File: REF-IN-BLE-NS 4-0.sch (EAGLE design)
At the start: 44 parts, among them U1 NRF52832_10QFN48, U2 AEM10941, X1 FA-128-32MHZMF10Z-AJ5

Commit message: Added caps and prettied up
Documentation is still needed, will add that as an issue
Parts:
- added C17, C18: 12pF, resistor:C-USC0603
- added C19, C20: 220uF, resistor:C-USC1206
- added C21, C22, C23, C24, C25: (no value), resistor:C-USC1206
- added C26, C27, C28, C29, C30: (no value), resistor:C-USC1210
- added U$11: SOLDER_BRIGDECLOSED, 00_PF_Nordic:SOLDER_BRIGDECLOSED
- added U$12, U$13, U$14, U$15, U$16, U$17, U$18, U$19, U$20, U$21, U$22: 1MM_PAD, 00_PF_Nordic:1MM_PAD
- added U$23: CAP-XX_A-TYPE, 00_PF_Nordic:CAP-XX_A-TYPE
- added U$24: CAP-XX_S-TYPE, 00_PF_Nordic:CAP-XX_S-TYPE
- added U$25: CAP-XX_W-TYPE, 00_PF_Nordic:CAP-XX_W-TYPE
- added U$26: BZ01_L-TYPE, 00_PF_Nordic:BZ01_L-TYPE
- added U$27: BZ059_N-TYPE, 00_PF_Nordic:BZ059_N-TYPE
- added U$28: BZ01_S-TYPE, 00_PF_Nordic:BZ01_S-TYPE
- added U$29: BZ05_S-TYPE, 00_PF_Nordic:BZ05_S-TYPE
- added U$30: BZ09_S-TYPE, 00_PF_Nordic:BZ09_S-TYPE
- added X2: 32.768k, 00_PF_Nordic:FC-135_32.7680KA-AC
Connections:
- removed net N$34: U2.BAL
- new net BAL: U$11.P1, U$19.P$1, U$23.BAL, U$24.BAL, U$25.BAL, U$26.2, U$28.2, U$29.2, U$30.2, U2.BAL
- new net BATT: C19.1, C20.1, C21.1, C22.1, C23.1, C24.1, C25.1, C26.1, C27.1, C28.1, C29.1, C30.1, U$18.P$1, U$23.+, U$24.+, U$25.+, U$26.1, U$27.1, U$28.1, U$29.1, U$30.1, U2.BATT
- new net N$36: C17.1, U1.P0_XL1, X2.P$1
- new net N$37: C18.1, U1.P1_XL2, X2.P$2
- new net N$38: U$20.P$1, U1.P2_AIN0
- new net N$39: U$13.P$1, U2.STATUS2
- new net N$40: U$14.P$1, U2.STATUS1
- new net N$41: U$15.P$1, U2.STATUS0
- new net N$42: U$21.P$1, U1.P3_AIN1
- new net N$43: U$22.P$1, U1.P4_AIN2
- net GND: now also C17.2, C18.2, C19.2, C20.2, C21.2, C22.2, C23.2, C24.2, C25.2, C26.2, C27.2, C28.2, C29.2, C30.2, U$11.P2, U$17.P$1, U$23.-, U$24.-, U$25.-, U$27.2
- net LVOUT: now also U$16.P$1
- net N$33: now also U$12.P$1, U2.PRIM; no longer U2.BATT
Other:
- note added: "1206 Footprints"
- note added: "1210 Footprints"
- note added: "AVX Super-capacitors"
- note added: "CAP-XX Super-capacitors"
- moved on the sheet: L4, R1, R10, R2, R3, R4, R5, R6, R9, U$1, U2

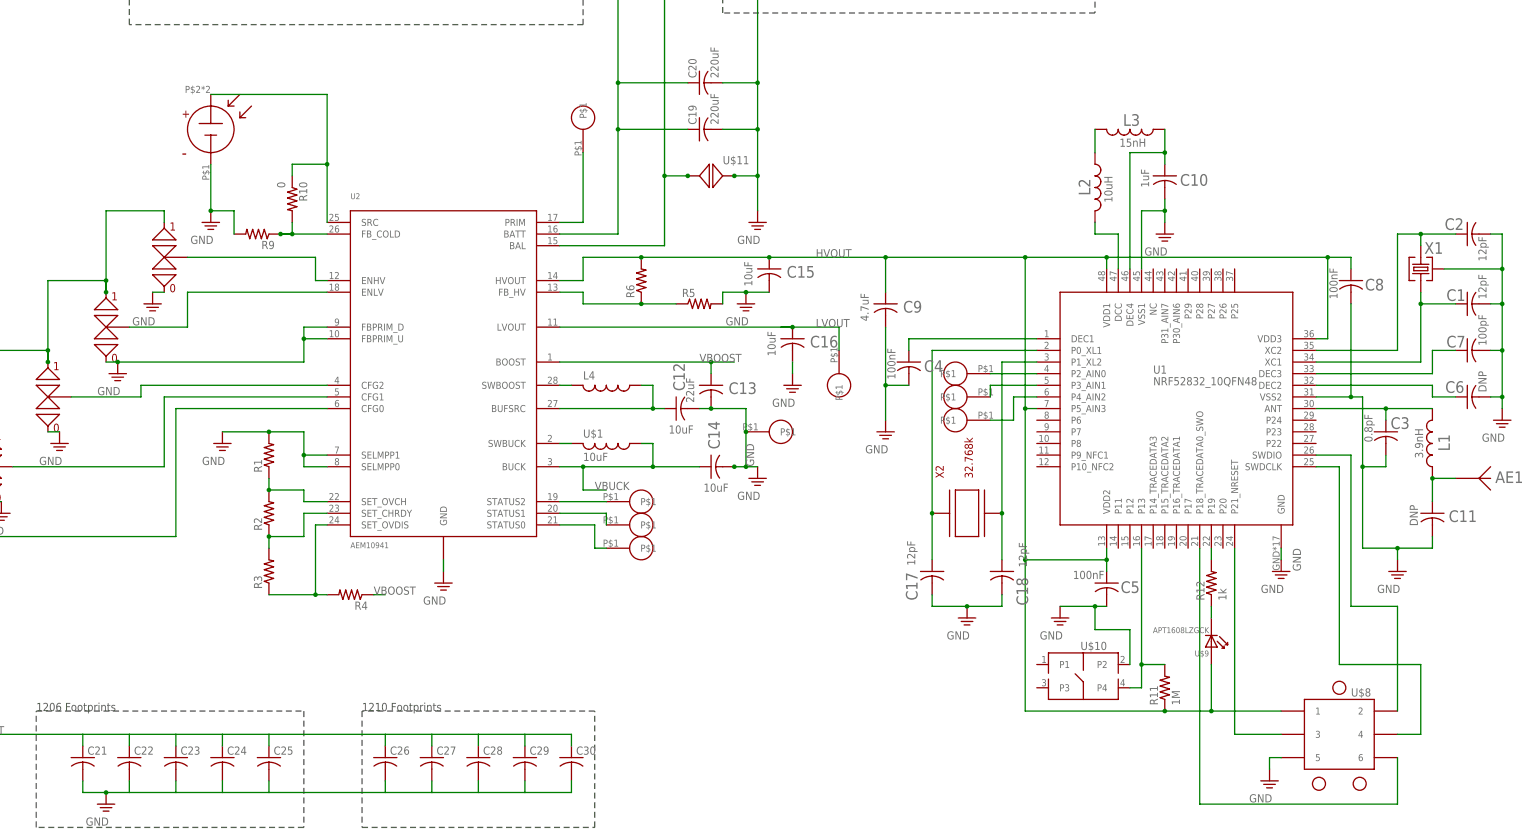
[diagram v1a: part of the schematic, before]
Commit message: Fixed grounding and added labels
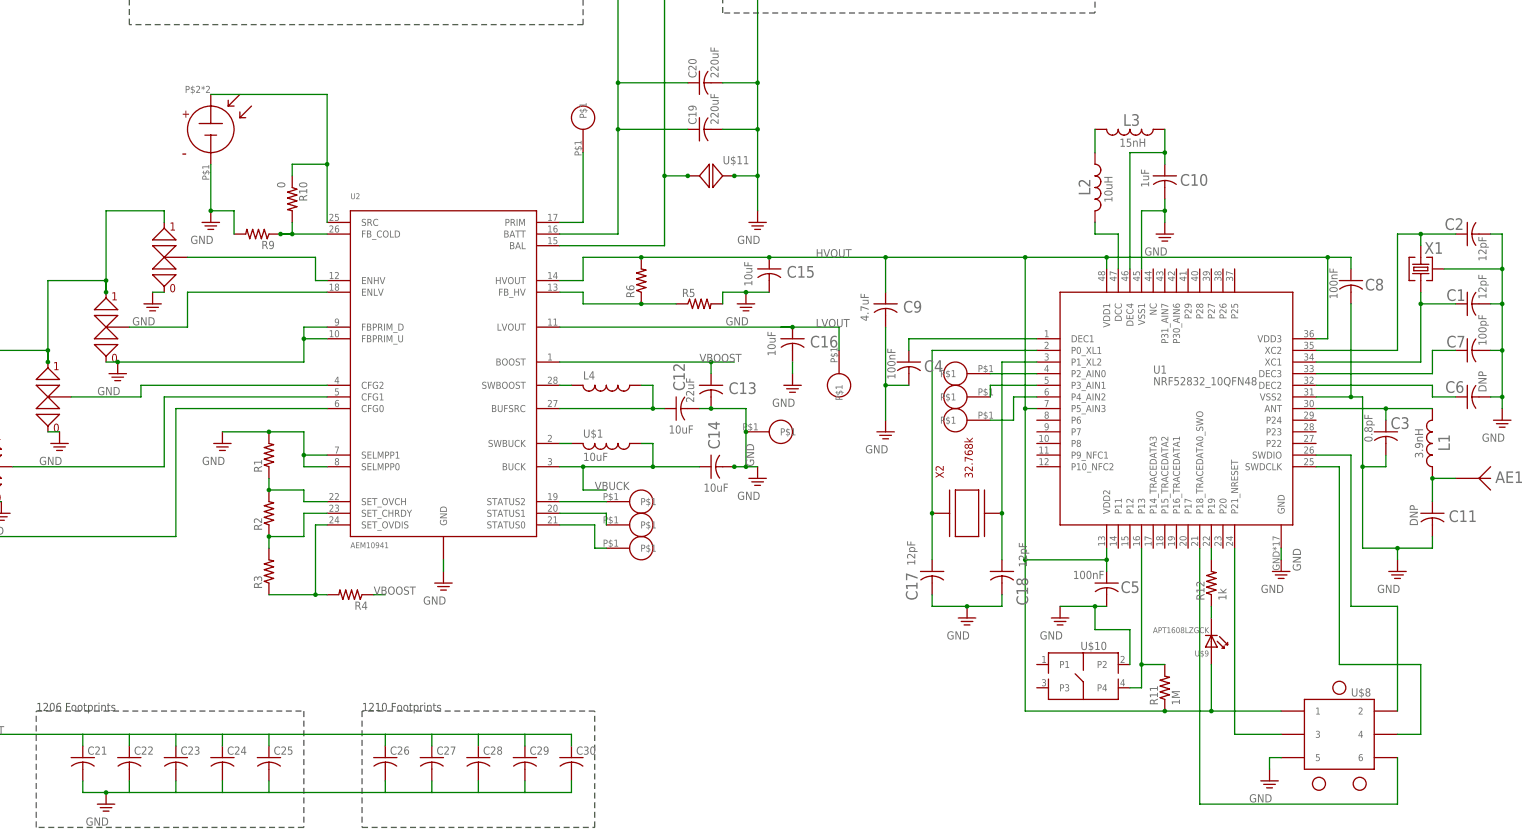
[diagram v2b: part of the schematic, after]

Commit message: Modified top cream
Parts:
- L4: value (none) -> 22uH
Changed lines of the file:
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@@
 <part name="G16" library="supply2" deviceset="PE" device="" value="GND"/>
 <part name="U$7" library="00_PF_Nordic" deviceset="SOLAR_CELL" device=""/>
-<part name="L4" library="00_PF_Nordic" deviceset="744031220" device=""/>
+<part name="L4" library="00_PF_Nordic" deviceset="744031220" device="" value="22uH"/>
 <part name="U$8" library="00_PF_Nordic" deviceset="TC2030-IDC" device=""/>
 <part name="G17" library="supply2" deviceset="PE" device="" value="GND"/>

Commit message: Added MPNs to Device Technologies
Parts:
- C1, C17, C18, C2: device resistor:C-USC0603 -> resistor:C-UST-12PFC0603
- C10: device resistor:C-USC0603 -> resistor:C-UST-1UFC0603; PERCENTAGE (none) -> 10%
- C12, C14, C15, C16: device resistor:C-USC0603 -> resistor:C-UST-10UFC0603
- C13: device resistor:C-USC0603 -> resistor:C-UST-22UFC0603
- C19, C20: device resistor:C-USC1206 -> resistor:C-UST-220UFC1206
- C3: device resistor:C-USC0603 -> resistor:C-UST-0.8PFC0603
- C4, C5, C8: device resistor:C-USC0603 -> resistor:C-UST-100NFC0603
- C7: device resistor:C-USC0603 -> resistor:C-UST-100PFC0603
- C9: device resistor:C-USC0603 -> resistor:C-UST-4.7UFC0603
- L1: device 00_PF_Nordic:L0603 -> 00_PF_Nordic:L0603V-3.9NH
- L2: device 00_PF_Nordic:L0603 -> 00_PF_Nordic:L0603V-10UH
- L3: device 00_PF_Nordic:L0603 -> 00_PF_Nordic:L0603V-15NH
- R10: device resistor:R-US_M0805 -> resistor:R-US_T-0OHMR0805
- R11: device resistor:R-US_M0805 -> resistor:R-US_T-1MOHMR0805
- R12: device resistor:R-US_M0805 -> resistor:R-US_T-1KOHMR0805
- U$1: value 10uF -> 10uH; device 00_PF_Nordic:L1007 -> 00_PF_Nordic:L0603V-10UH; MFG_PART# (none) -> L1007C101KPWST
- U$9: value APT1608LZGCK -> N/A
- X1: value FA-128-32MHZMF10Z-AJ5 -> 32 MHz
- X2: value 32.768k -> 32.768 kHz
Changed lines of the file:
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@@
 <parts>
 <part name="U1" library="00_PF_Nordic" deviceset="NRF52832_10QFN48" device=""/>
-<part name="C1" library="resistor" deviceset="C-US" device="C0603" value="12pF"/>
-<part name="L3" library="00_PF_Nordic" deviceset="L0603" device="" value="15nH"/>
-<part name="L2" library="00_PF_Nordic" deviceset="L0603" device="" value="10uH"/>
-<part name="L1" library="00_PF_Nordic" deviceset="L0603" device="" value="3.9nH"/>
-<part name="C2" library="resistor" deviceset="C-US" device="C0603" value="12pF"/>
-<part name="C3" library="resistor" deviceset="C-US" device="C0603" value="0.8pF"/>
-<part name="C4" library="resistor" deviceset="C-US" device="C0603" value="100nF"/>
-<part name="C5" library="resistor" deviceset="C-US" device="C0603" value="100nF"/>
+<part name="C1" library="resistor" deviceset="C-US" device="C0603" technology="T-12PF" value="12pF"/>
+<part name="L3" library="00_PF_Nordic" deviceset="L0603" device="" technology="V-15NH" value="15nH"/>
+<part name="L2" library="00_PF_Nordic" deviceset="L0603" device="" technology="V-10UH" value="10uH"/>
+<part name="L1" library="00_PF_Nordic" deviceset="L0603" device="" technology="V-3.9NH" value="3.9nH"/>
+<part name="C2" library="resistor" deviceset="C-US" device="C0603" technology="T-12PF" value="12pF"/>
+<part name="C3" library="resistor" deviceset="C-US" device="C0603" technology="T-0.8PF" value="0.8pF"/>
+<part name="C4" library="resistor" deviceset="C-US" device="C0603" technology="T-100NF" value="100nF"/>
+<part name="C5" library="resistor" deviceset="C-US" device="C0603" technology="T-100NF" value="100nF"/>
 <part name="C6" library="resistor" deviceset="C-US" device="C0603" value="DNP"/>
-<part name="C7" library="resistor" deviceset="C-US" device="C0603" value="100pF"/>
-<part name="C8" library="resistor" deviceset="C-US" device="C0603" value="100nF"/>
-<part name="C9" library="resistor" deviceset="C-US" device="C0603" value="4.7uF"/>
-<part name="C10" library="resistor" deviceset="C-US" device="C0603" value="1uF"/>
+<part name="C7" library="resistor" deviceset="C-US" device="C0603" technology="T-100PF" value="100pF"/>
+<part name="C8" library="resistor" deviceset="C-US" device="C0603" technology="T-100NF" value="100nF"/>
+<part name="C9" library="resistor" deviceset="C-US" device="C0603" technology="T-4.7UF" value="4.7uF"/>
+<part name="C10" library="resistor" deviceset="C-US" device="C0603" technology="T-1UF" value="1uF">
+<attribute name="PERCENTAGE" value="10%"/>
+</part>
 <part name="G1" library="supply2" deviceset="PE" device="" value="GND"/>
 <part name="G2" library="supply2" deviceset="PE" device="" value="GND"/>
 <part name="G3" library="supply2" deviceset="PE" device="" value="GND"/>
-<part name="X1" library="00_PF_Nordic" deviceset="FA-128-32MHZMF10Z-AJ5" device=""/>
+<part name="X1" library="00_PF_Nordic" deviceset="FA-128-32MHZMF10Z-AJ5" device="" value="32 MHz"/>
 <part name="G5" library="supply2" deviceset="PE" device="" value="GND"/>
 <part name="G6" library="supply2" deviceset="PE" device="" value="GND"/>
@@
 <part name="C11" library="resistor" deviceset="C-US" device="C0603" value="DNP"/>
 <part name="U2" library="00_PF_Nordic" deviceset="AEM10941" device=""/>
-<part name="C12" library="resistor" deviceset="C-US" device="C0603" value="10uF"/>
+<part name="C12" library="resistor" deviceset="C-US" device="C0603" technology="T-10UF" value="10uF"/>
 <part name="G4" library="supply2" deviceset="PE" device="" value="GND"/>
-<part name="C13" library="resistor" deviceset="C-US" device="C0603" value="22uF"/>
-<part name="C14" library="resistor" deviceset="C-US" device="C0603" value="10uF"/>
-<part name="C15" library="resistor" deviceset="C-US" device="C0603" value="10uF"/>
-<part name="C16" library="resistor" deviceset="C-US" device="C0603" value="10uF"/>
+<part name="C13" library="resistor" deviceset="C-US" device="C0603" technology="T-22UF" value="22uF"/>
+<part name="C14" library="resistor" deviceset="C-US" device="C0603" technology="T-10UF" value="10uF"/>
+<part name="C15" library="resistor" deviceset="C-US" device="C0603" technology="T-10UF" value="10uF"/>
+<part name="C16" library="resistor" deviceset="C-US" device="C0603" technology="T-10UF" value="10uF"/>
 <part name="G7" library="supply2" deviceset="PE" device="" value="GND"/>
 <part name="G8" library="supply2" deviceset="PE" device="" value="GND"/>
 <part name="G9" library="supply2" deviceset="PE" device="" value="GND"/>
-<part name="U$1" library="00_PF_Nordic" deviceset="L1007" device="" value="10uF"/>
+<part name="U$1" library="00_PF_Nordic" deviceset="L0603" device="" technology="V-10UH" value="10uH">
+<attribute name="MFG_PART#" value="L1007C101KPWST"/>
+</part>
 <part name="R1" library="resistor" deviceset="R-US_" device="M0805"/>
 <part name="R2" library="resistor" deviceset="R-US_" device="M0805"/>
@@
 <part name="R6" library="resistor" deviceset="R-US_" device="M0805"/>
 <part name="R9" library="resistor" deviceset="R-US_" device="M0805"/>
-<part name="R10" library="resistor" deviceset="R-US_" device="M0805" value="0"/>
+<part name="R10" library="resistor" deviceset="R-US_" device="R0805" technology="T-0OHM" value="0"/>
 <part name="G16" library="supply2" deviceset="PE" device="" value="GND"/>
 <part name="U$7" library="00_PF_Nordic" deviceset="SOLAR_CELL" device=""/>
@@
 <part name="G17" library="supply2" deviceset="PE" device="" value="GND"/>
 <part name="G18" library="supply2" deviceset="PE" device="" value="GND"/>
-<part name="U$9" library="00_PF_Nordic" deviceset="APT1608LZGCK" device=""/>
-<part name="U$10" library="00_PF_Nordic" deviceset="MJTP1140" device=""/>
-<part name="R11" library="resistor" deviceset="R-US_" device="M0805" value="1M"/>
-<part name="R12" library="resistor" deviceset="R-US_" device="M0805" value="1k"/>
+<part name="U$9" library="00_PF_Nordic" deviceset="APT1608LZGCK" device="" value="N/A"/>
+<part name="U$10" library="00_PF_Nordic" deviceset="MJTP1140" device="" value=""/>
+<part name="R11" library="resistor" deviceset="R-US_" device="R0805" technology="T-1MOHM" value="1M"/>
+<part name="R12" library="resistor" deviceset="R-US_" device="R0805" technology="T-1KOHM" value="1k"/>
 <part name="G19" library="supply2" deviceset="PE" device="" value="GND"/>
 <part name="U$11" library="00_PF_Nordic" deviceset="SOLDER_BRIGDE" device="CLOSED"/>
-<part name="C17" library="resistor" deviceset="C-US" device="C0603" value="12pF"/>
-<part name="C18" library="resistor" deviceset="C-US" device="C0603" value="12pF"/>
+<part name="C17" library="resistor" deviceset="C-US" device="C0603" technology="T-12PF" value="12pF"/>
+<part name="C18" library="resistor" deviceset="C-US" device="C0603" technology="T-12PF" value="12pF"/>
 <part name="G20" library="supply2" deviceset="PE" device="" value="GND"/>
-<part name="X2" library="00_PF_Nordic" deviceset="FC-135_32.7680KA-AC" device="" value="32.768k"/>
+<part name="X2" library="00_PF_Nordic" deviceset="FC-135_32.7680KA-AC" device="" value="32.768 kHz"/>
 <part name="U$12" library="00_PF_Nordic" deviceset="1MM_PAD" device=""/>
 <part name="U$13" library="00_PF_Nordic" deviceset="1MM_PAD" device=""/>
@@
 <part name="U$21" library="00_PF_Nordic" deviceset="1MM_PAD" device=""/>
 <part name="U$22" library="00_PF_Nordic" deviceset="1MM_PAD" device=""/>
-<part name="C19" library="resistor" deviceset="C-US" device="C1206" value="220uF"/>
-<part name="C20" library="resistor" deviceset="C-US" device="C1206" value="220uF"/>
+<part name="C19" library="resistor" deviceset="C-US" device="C1206" technology="T-220UF" value="220uF"/>
+<part name="C20" library="resistor" deviceset="C-US" device="C1206" technology="T-220UF" value="220uF"/>
 <part name="U$23" library="00_PF_Nordic" deviceset="CAP-XX_A-TYPE" device=""/>
 <part name="U$24" library="00_PF_Nordic" deviceset="CAP-XX_S-TYPE" device=""/>
@@
 <attribute name="VALUE" x="-15.748" y="-35.433" size="1.778" layer="96" rot="R180"/>
 </instance>
-<instance part="C6" gate="G$1" x="63.5" y="2.54" smashed="yes" rot="R90">
-<attribute name="NAME" x="58.674" y="3.429" size="2.54" layer="95"/>
-<attribute name="VALUE" x="67.691" y="3.556" size="1.778" layer="96" rot="R90"/>
-</instance>
+<instance part="C6" gate="G$1" x="63.5" y="2.54" rot="R90"/>
 <instance part="C7" gate="G$1" x="63.5" y="12.7" smashed="yes" rot="R90">
 <attribute name="NAME" x="58.928" y="13.335" size="2.54" layer="95"/>
@@
 <instance part="G8" gate="PE" x="-93.98" y="22.86"/>
 <instance part="G9" gate="PE" x="-160.02" y="-38.1"/>
-<instance part="U$1" gate="G$1" x="-124.46" y="-7.62" rot="R270"/>
+<instance part="U$1" gate="G$1" x="-124.46" y="-7.62" rot="R270">
+<attribute name="MFG_PART#" x="-124.46" y="-7.62" size="1.778" layer="96" rot="R270" display="off"/>
+</instance>
 <instance part="R1" gate="G$1" x="-198.12" y="-10.16" rot="R90"/>
 <instance part="R2" gate="G$1" x="-198.12" y="-22.86" rot="R90"/>

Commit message: Changed MPN for U$1
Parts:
- U$1: MFG_PART# L1007C101KPWST -> (none)
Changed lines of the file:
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@@
 <part name="G8" library="supply2" deviceset="PE" device="" value="GND"/>
 <part name="G9" library="supply2" deviceset="PE" device="" value="GND"/>
-<part name="U$1" library="00_PF_Nordic" deviceset="L0603" device="" technology="V-10UH" value="10uH">
-<attribute name="MFG_PART#" value="L1007C101KPWST"/>
-</part>
+<part name="U$1" library="00_PF_Nordic" deviceset="L0603" device="" technology="V-10UH" value="10uH"/>
 <part name="R1" library="resistor" deviceset="R-US_" device="M0805"/>
 <part name="R2" library="resistor" deviceset="R-US_" device="M0805"/>

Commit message: Second revision of board Added LDO bypass circuit to attempt to get a higher efficiency from the charge capacitors. Added a way to break away solar from the rest of the assembly. Moved pin connectors to processing side of the board Swapped 0805 components for 0603 Moved the capacitor bank to the processing side of the board Rerouted some signals to fit everything nicely
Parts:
- removed C26, C27, C28, C29, C30: (no value), resistor:C-USC1210
- added R7: 1M, resistor:R-US_R0603
- added RTEST: (no value), resistor:R-US_R0603
- added U$31: DOUBLE_SOLDER_BRIDGE1_CLOSED, 00_PF_Nordic:DOUBLE_SOLDER_BRIDGE1_CLOSED
- added U$32: SOLDER_BRIGDECLOSED, 00_PF_Nordic:SOLDER_BRIGDECLOSED
- added U$33: DMG2305U-13, 00-PF-DevKits:DMG2305U-13
- added U$34: DMG2302UK-13, 00_PF_Nordic:DMG2302UK-13
- added U$35, U$36, U$37, U$38, U$39, U$40, U$41: N/A, 00_PF_Nordic:1MM_PAD
- AE1: value 2.4GHZ_ANTENNA -> N/A
- R1, R2, R3, R4, R5, R6, R9: device resistor:R-US_M0805 -> resistor:R-US_R0603
- R10: device resistor:R-US_T-0OHMR0805 -> resistor:R-US_R0603
- R11: device resistor:R-US_T-1MOHMR0805 -> resistor:R-US_R0603
- R12: device resistor:R-US_T-1KOHMR0805 -> resistor:R-US_R0603
- U$12, U$13, U$14, U$15, U$16, U$17, U$18, U$19, U$20, U$21, U$22: value 1MM_PAD -> N/A
- U$23: value CAP-XX_A-TYPE -> N/A
- U$24: value CAP-XX_S-TYPE -> N/A
- U$25: value CAP-XX_W-TYPE -> N/A
- U$26: value BZ01_L-TYPE -> N/A
- U$27: value BZ059_N-TYPE -> N/A
- U$28: value BZ01_S-TYPE -> N/A
- U$29: value BZ05_S-TYPE -> N/A
- U$30: value BZ09_S-TYPE -> N/A
- U$4: value DOUBLE_SOLDER_BRIDGE0_CLOSED -> N/A
- U$7: value SOLAR_CELL -> N/A
- U$8: value TC2030-IDC -> N/A
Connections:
- net N$33 renamed PRIM
- net N$39 renamed STATUS2
- net N$40 renamed STATUS1
- removed net N$41: U$15.P$1, U2.STATUS0
- new net N$34: C15.1, R6.2, U$31.IN0, U$37.P$1, U2.HVOUT
- new net N$45: RTEST.2, U$31.OUT, U$32.P2
- new net N$46: U$31.IN1, U$33.D
- new net N$47: R7.1, U$33.G, U$34.D
- new net STATUS0: U$15.P$1, U$34.G, U2.STATUS0
- net BAL: now also U$41.P$1
- net BATT: now also R7.2, U$33.S, U$40.P$1; no longer C26.1, C27.1, C28.1, C29.1, C30.1
- net GND: now also RTEST.1, U$34.S, U$35.P$1, U$38.P$1; no longer C26.2, C27.2, C28.2, C29.2, C30.2
- net HVOUT: now also U$32.P1; no longer C15.1, R6.2, U2.HVOUT
- net N$29: now also U$36.P$1, U$39.P$1
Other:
- note removed: "1210 Footprints"
- moved on the sheet: AE1, C1, C10, C11, C17, C18, C2, C3, C4, C5, C6, C7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
